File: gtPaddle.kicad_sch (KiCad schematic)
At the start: 57 parts, among them IC1 74157N, Q1 2N3904, Q10 2N3906, Q11 2N3904, Q12 2N3906, Q13 2N3904, Q14 2N3904, Q2 2N3904, Q3 2N3904, Q4 2N3904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

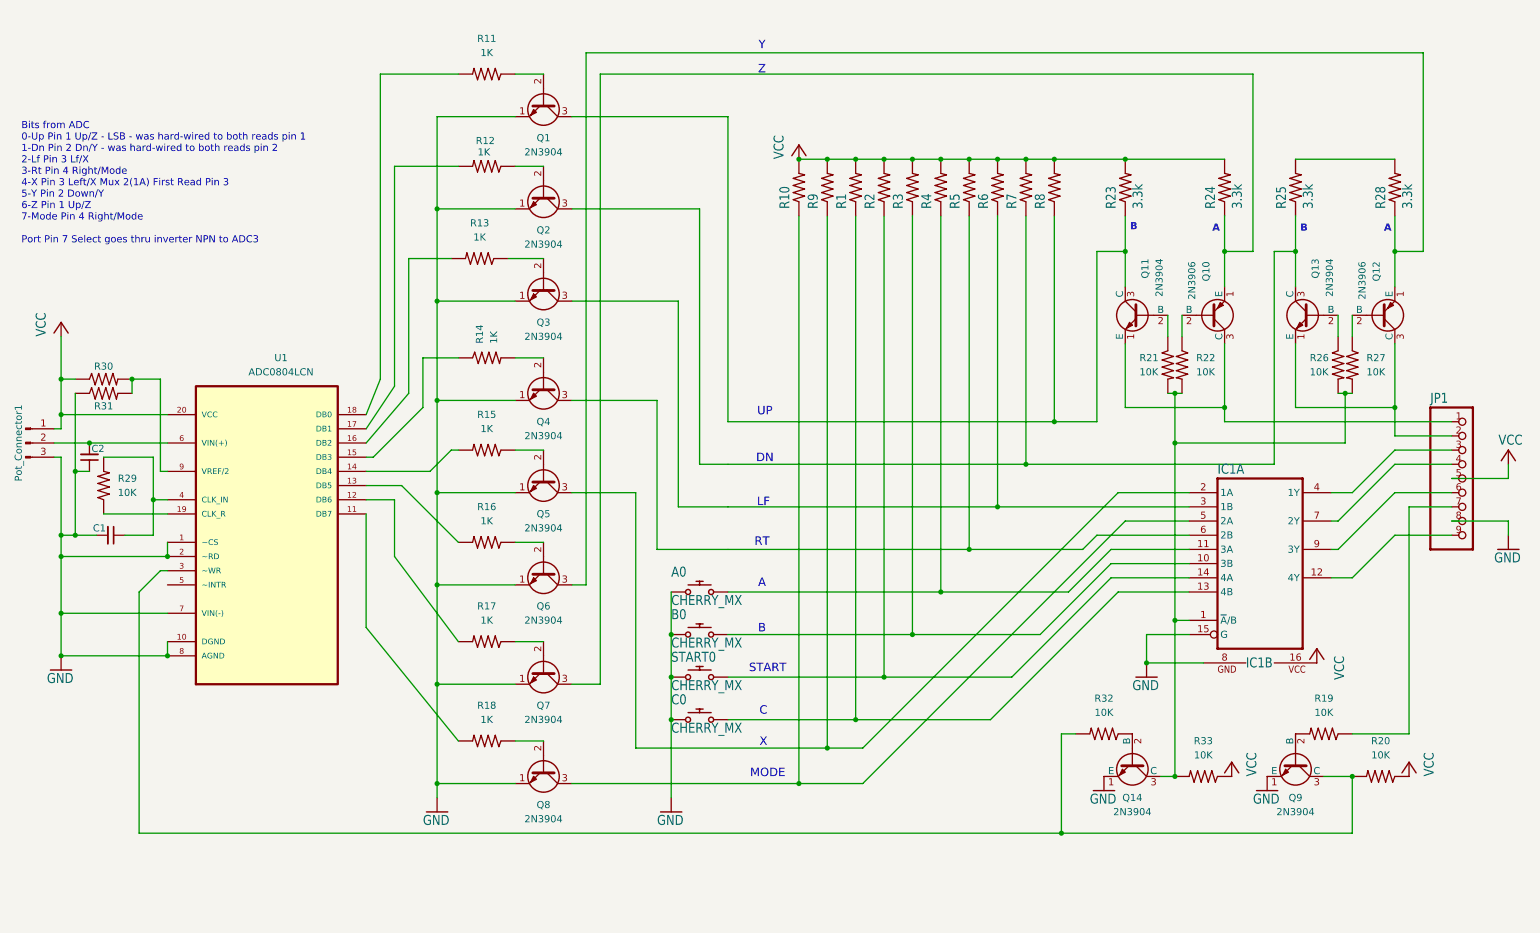
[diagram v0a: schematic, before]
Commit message: much simplified design
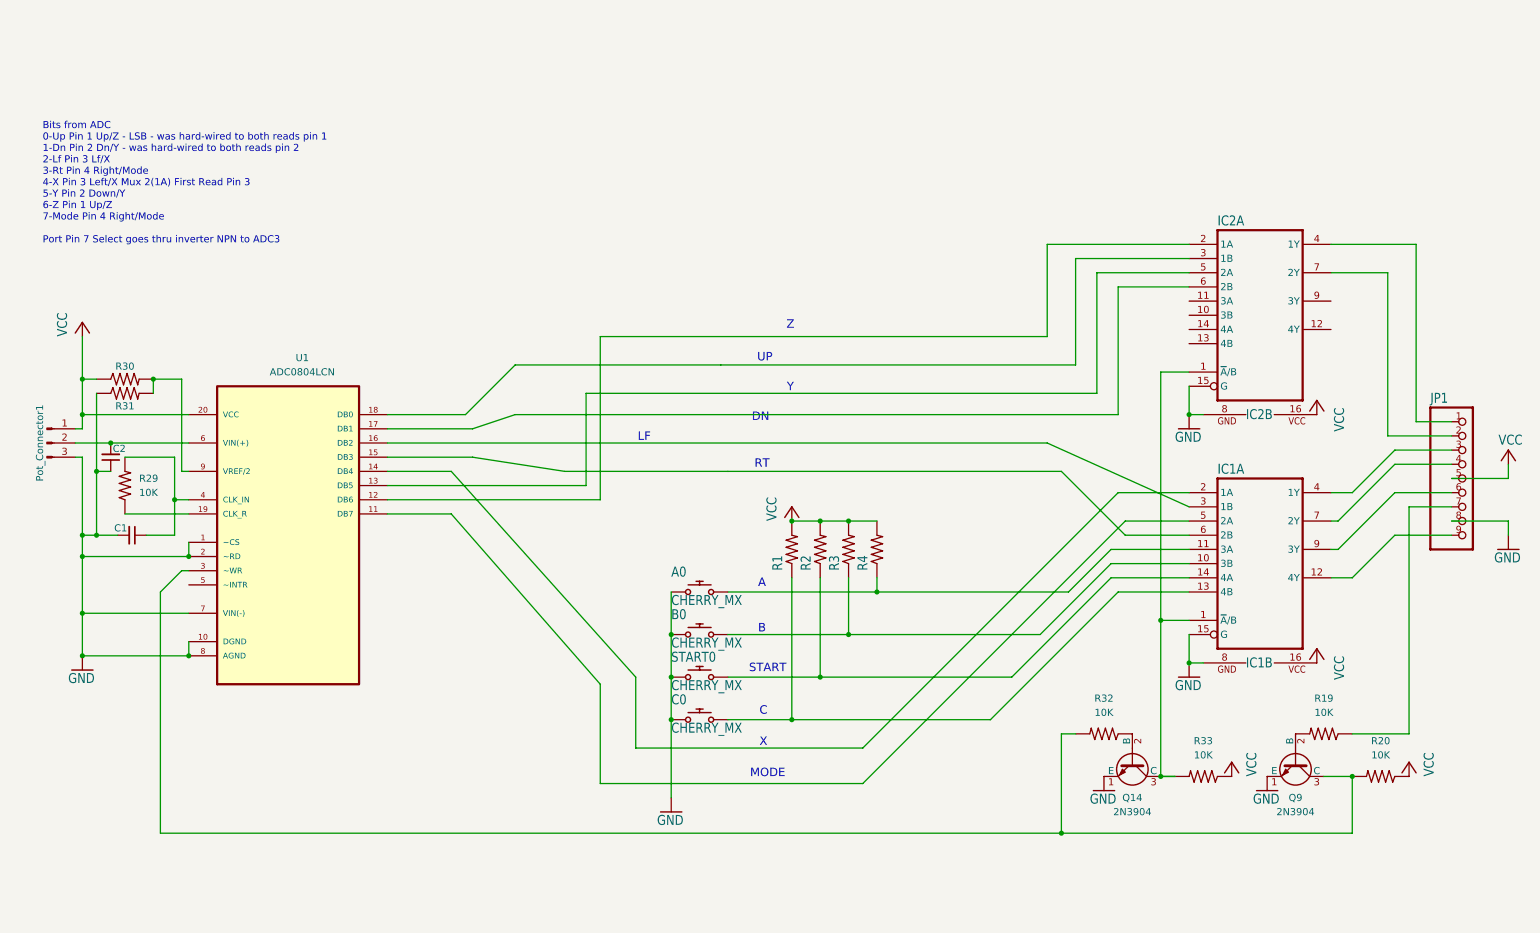
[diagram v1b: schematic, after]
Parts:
- removed Q1, Q11, Q13, Q2, Q3, Q4, Q5, Q6, Q7, Q8: 2N3904, Package_TO_SOT_THT:TO-92_Inline, symbol Transistor_BJT:2N3904
- removed Q10, Q12: 2N3906, Package_TO_SOT_THT:TO-92_Inline, symbol Transistor_BJT:2N3906
- removed R10, R23, R24, R25, R28, R5, R6, R7, R8, R9: 3.3k, gpad1:0207_10, symbol gpad1-eagle-import:R-US_0207/10
- removed R11, R12, R13, R14, R15, R16, R17, R18: 1K, gpad1:0207_10, symbol gpad1-eagle-import:R-US_0207/10
- removed R21, R22, R26, R27: 10K, gpad1:0207_10, symbol gpad1-eagle-import:R-US_0207/10
- added IC2: 74157N, gpad1:DIL16, symbol gpad1-eagle-import:74157N
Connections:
- net GND: now also IC2.15 (G), IC2.8 (GND)
- net VCC: now also IC2.16 (VCC)
- net at IC1.3 (1B): now also U1.16 (DB2)
- net at IC1.1 (~{A}/B), Q14.3 (C), R33.2: now also IC2.1 (~{A}/B)
- net at JP1.1: now also IC2.4 (1Y)
- net at IC1.2 (1A): now also U1.14 (DB4)
- net at U1.13 (DB5): now also IC2.5 (2A)
- net at IC1.5 (2A): now also U1.11 (DB7)
- net at U1.12 (DB6): now also IC2.2 (1A)
- net at U1.17 (DB1): now also IC2.6 (2B)
- net at U1.15 (DB3): now also IC1.6 (2B)
- net at U1.18 (DB0): now also IC2.3 (1B)
- net at JP1.2: now also IC2.7 (2Y)
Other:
- moved on the sheet: C1, C2, Pot_Connector1, R1, R2, R29, R3, R30, R31, R4, U1

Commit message: more simplified
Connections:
- net GND: now also IC2.10 (3B), IC2.11 (3A), IC2.12 (4Y), IC2.13 (4B), IC2.14 (4A), IC2.9 (3Y)
- net at IC1.1 (~{A}/B), IC2.1 (~{A}/B), Q14.3 (C)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: now also IC2.6 (2B), U1.17 (DB1)
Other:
- note added: "Bits from ADC 0-Up Pin 1 Up 1-Dn Pin 2 Dn 2-Lf Pin 3 Lf 3-Rt Pin 4 Right 4-X Pin 3 X Mux 5-Y Pin 2 Y 6-Z Pin 1 Z 7-Mode Pin 4 Mode Port Pin 7 Select goes thru inverter NPN to ADC3 Second inverter as buffer for select just in case"
- note removed: "Bits from ADC 0-Up Pin 1 Up/Z - LSB - was hard-wired to both reads pin 1 1-Dn Pin 2 Dn/Y - was hard-wired to both reads pin 2 2-Lf Pin 3 Lf/X 3-Rt Pin 4 Right/Mode 4-X Pin 3 Left/X Mux 2(1A) First Read Pin 3 5-Y Pin 2 Down/Y 6-Z Pin 1 Up/Z 7-Mode Pin 4 Right/Mode Port Pin 7 Select goes thru inverter NPN to ADC3"
- moved on the sheet: A0, B0, C0, C1, C2, IC1A, IC1B, IC2A, IC2B, JP1, Pot_Connector1, Q14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

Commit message: some wire cleanup
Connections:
- net at IC1.1 (~{A}/B), IC2.1 (~{A}/B), Q14.3 (C)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: no longer IC2.6 (2B), U1.17 (DB1)
- new net: IC2.6 (2B), U1.17 (DB1)
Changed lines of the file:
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@@
 	(text "MODE"
 		(exclude_from_sim no)
-		(at 136.652 88.392 0)
+		(at 135.636 85.344 0)
 		(effects
 			(font
@@
 	(text "RT"
 		(exclude_from_sim no)
-		(at 134.366 78.74 0)
+		(at 134.366 76.962 0)
 		(effects
 			(font
@@
 	(text "X"
 		(exclude_from_sim no)
-		(at 134.62 82.55 0)
+		(at 134.366 80.264 0)
 		(effects
 			(font
@@
 	(text "DN"
 		(exclude_from_sim no)
-		(at 134.112 67.818 0)
+		(at 134.62 64.516 0)
 		(effects
 			(font
@@
 	(text "LF"
 		(exclude_from_sim no)
-		(at 113.284 75.184 0)
+		(at 134.366 72.39 0)
 		(effects
 			(font
@@
 	)
 	(junction
-		(at 205.74 67.31)
-		(diameter 0)
-		(color 0 0 0 0)
-	)
-	(junction
 		(at 187.96 146.05)
 		(diameter 0)
@@
 	)
 	(junction
-		(at 205.74 63.5)
-		(diameter 0)
-		(color 0 0 0 0)
-	)
-	(junction
 		(at 118.11 124.46)
 		(diameter 0)
@@
 	(wire
 		(pts
+			(xy 196.85 64.77) (xy 196.85 57.15)
+		)
+		(stroke
+			(width 0)
+			(type default)
+		)
+	)
+	(wire
+		(pts
 			(xy 39.37 54.61) (xy 58.42 54.61)
 		)
@@
 	(wire
 		(pts
-			(xy 102.87 62.23) (xy 194.31 62.23)
+			(xy 120.65 62.23) (xy 194.31 62.23)
 		)
 		(stroke
@@
 	(wire
 		(pts
-			(xy 205.74 67.31) (xy 205.74 63.5)
+			(xy 190.5 86.36) (xy 194.31 90.17)
 		)
 		(stroke
@@
 	(wire
 		(pts
+			(xy 194.31 85.09) (xy 210.82 85.09)
+		)
+		(stroke
+			(width 0)
+			(type default)
+		)
+	)
+	(wire
+		(pts
 			(xy 240.03 100.33) (xy 247.65 92.71)
 		)
@@
 	(wire
 		(pts
-			(xy 114.3 85.09) (xy 93.98 64.77)
+			(xy 110.49 81.28) (xy 93.98 64.77)
 		)
 		(stroke
@@
 	(wire
 		(pts
+			(xy 196.85 57.15) (xy 205.74 48.26)
+		)
+		(stroke
+			(width 0)
+			(type default)
+		)
+	)
+	(wire
+		(pts
 			(xy 57.15 64.77) (xy 58.42 64.77)
 		)
@@
 	(wire
 		(pts
-			(xy 93.98 72.39) (xy 97.79 72.39)
+			(xy 93.98 72.39) (xy 95.25 72.39)
 		)
 		(stroke
@@
 	(wire
 		(pts
-			(xy 97.79 58.42) (xy 134.62 58.42)
+			(xy 111.76 58.42) (xy 134.62 58.42)
 		)
 		(stroke
@@
 	(wire
 		(pts
-			(xy 205.74 63.5) (xy 205.74 48.26)
-		)
-		(stroke
-			(width 0)
-			(type default)
-		)
-	)
-	(wire
-		(pts
 			(xy 194.31 62.23) (xy 194.31 45.72)
 		)
@@
 	(wire
 		(pts
-			(xy 110.49 78.74) (xy 93.98 62.23)
+			(xy 113.03 77.47) (xy 96.52 62.23)
 		)
 		(stroke
@@
 	(wire
 		(pts
-			(xy 97.79 58.42) (xy 93.98 54.61)
-		)
-		(stroke
-			(width 0)
-			(type default)
-		)
-	)
-	(wire
-		(pts
-			(xy 110.49 78.74) (xy 175.26 78.74)
+			(xy 111.76 58.42) (xy 107.95 54.61)
+		)
+		(stroke
+			(width 0)
+			(type default)
+		)
+	)
+	(wire
+		(pts
+			(xy 113.03 77.47) (xy 167.64 77.47)
 		)
 		(stroke
@@
 	(wire
 		(pts
-			(xy 205.74 67.31) (xy 205.74 107.95)
-		)
-		(stroke
-			(width 0.1524)
-			(type solid)
-		)
-	)
-	(wire
-		(pts
 			(xy 190.5 43.18) (xy 210.82 43.18)
 		)
@@
 	(wire
 		(pts
-			(xy 205.74 63.5) (xy 205.74 67.31)
+			(xy 205.74 63.5) (xy 205.74 107.95)
 		)
 		(stroke
@@
 	(wire
 		(pts
+			(xy 101.6 57.15) (xy 93.98 57.15)
+		)
+		(stroke
+			(width 0)
+			(type default)
+		)
+	)
+	(wire
+		(pts
+			(xy 194.31 85.09) (xy 190.5 81.28)
+		)
+		(stroke
+			(width 0)
+			(type default)
+		)
+	)
+	(wire
+		(pts
 			(xy 210.82 115.57) (xy 213.36 115.57)
 		)
@@
 	(wire
 		(pts
-			(xy 175.26 78.74) (xy 186.69 92.71)
+			(xy 167.64 77.47) (xy 179.07 92.71)
 		)
 		(stroke
@@
 	(wire
 		(pts
-			(xy 97.79 72.39) (xy 115.57 90.17)
+			(xy 95.25 72.39) (xy 113.03 86.36)
 		)
 		(stroke
@@
 	(wire
 		(pts
-			(xy 93.98 67.31) (xy 97.79 67.31)
+			(xy 93.98 67.31) (xy 115.57 67.31)
 		)
 		(stroke
@@
 	(wire
 		(pts
-			(xy 104.14 67.31) (xy 205.74 67.31)
+			(xy 110.49 64.77) (xy 196.85 64.77)
 		)
 		(stroke
@@
 	(wire
 		(pts
-			(xy 114.3 85.09) (xy 210.82 85.09)
+			(xy 110.49 81.28) (xy 190.5 81.28)
 		)
 		(stroke
@@
 	(wire
 		(pts
+			(xy 107.95 54.61) (xy 93.98 54.61)
+		)
+		(stroke
+			(width 0)
+			(type default)
+		)
+	)
+	(wire
+		(pts
 			(xy 234.95 135.89) (xy 240.03 135.89)
 		)
@@
 	(wire
 		(pts
-			(xy 104.14 67.31) (xy 93.98 57.15)
+			(xy 203.2 87.63) (xy 189.23 73.66)
+		)
+		(stroke
+			(width 0.1524)
+			(type solid)
+		)
+	)
+	(wire
+		(pts
+			(xy 110.49 64.77) (xy 101.6 57.15)
 		)
 		(stroke
@@
 	(wire
 		(pts
-			(xy 110.49 76.2) (xy 93.98 59.69)
-		)
-		(stroke
-			(width 0.1524)
-			(type solid)
-		)
-	)
-	(wire
-		(pts
-			(xy 200.66 90.17) (xy 210.82 90.17)
+			(xy 97.79 59.69) (xy 93.98 59.69)
+		)
+		(stroke
+			(width 0.1524)
+			(type solid)
+		)
+	)
+	(wire
+		(pts
+			(xy 114.3 73.66) (xy 97.79 59.69)
 		)
 		(stroke
@@
 	(wire
 		(pts
-			(xy 186.69 92.71) (xy 210.82 92.71)
-		)
-		(stroke
-			(width 0.1524)
-			(type solid)
-		)
-	)
-	(wire
-		(pts
-			(xy 115.57 90.17) (xy 200.66 90.17)
+			(xy 179.07 92.71) (xy 210.82 92.71)
+		)
+		(stroke
+			(width 0.1524)
+			(type solid)
+		)
+	)
+	(wire
+		(pts
+			(xy 113.03 86.36) (xy 190.5 86.36)
 		)
 		(stroke
@@
 	(wire
 		(pts
-			(xy 210.82 87.63) (xy 185.42 76.2)
-		)
-		(stroke
-			(width 0.1524)
-			(type solid)
-		)
-	)
-	(wire
-		(pts
 			(xy 144.78 106.68) (xy 144.78 124.46)
 		)
@@
 	(wire
 		(pts
-			(xy 97.79 67.31) (xy 102.87 62.23)
+			(xy 115.57 67.31) (xy 120.65 62.23)
 		)
 		(stroke
@@
 	(wire
 		(pts
-			(xy 110.49 76.2) (xy 185.42 76.2)
+			(xy 114.3 73.66) (xy 189.23 73.66)
 		)
 		(stroke
@@
 	(wire
 		(pts
+			(xy 203.2 87.63) (xy 210.82 87.63)
+		)
+		(stroke
+			(width 0.1524)
+			(type solid)
+		)
+	)
+	(wire
+		(pts
 			(xy 257.81 82.55) (xy 267.97 82.55)
 		)
@@
 	(wire
 		(pts
+			(xy 194.31 90.17) (xy 210.82 90.17)
+		)
+		(stroke
+			(width 0.1524)
+			(type solid)
+		)
+	)
+	(wire
+		(pts
 			(xy 44.45 59.69) (xy 58.42 59.69)
 		)
@@
 		)
 	)
+	(wire
+		(pts
+			(xy 96.52 62.23) (xy 93.98 62.23)
+		)
+		(stroke
+			(width 0.1524)
+			(type solid)
+		)
+	)

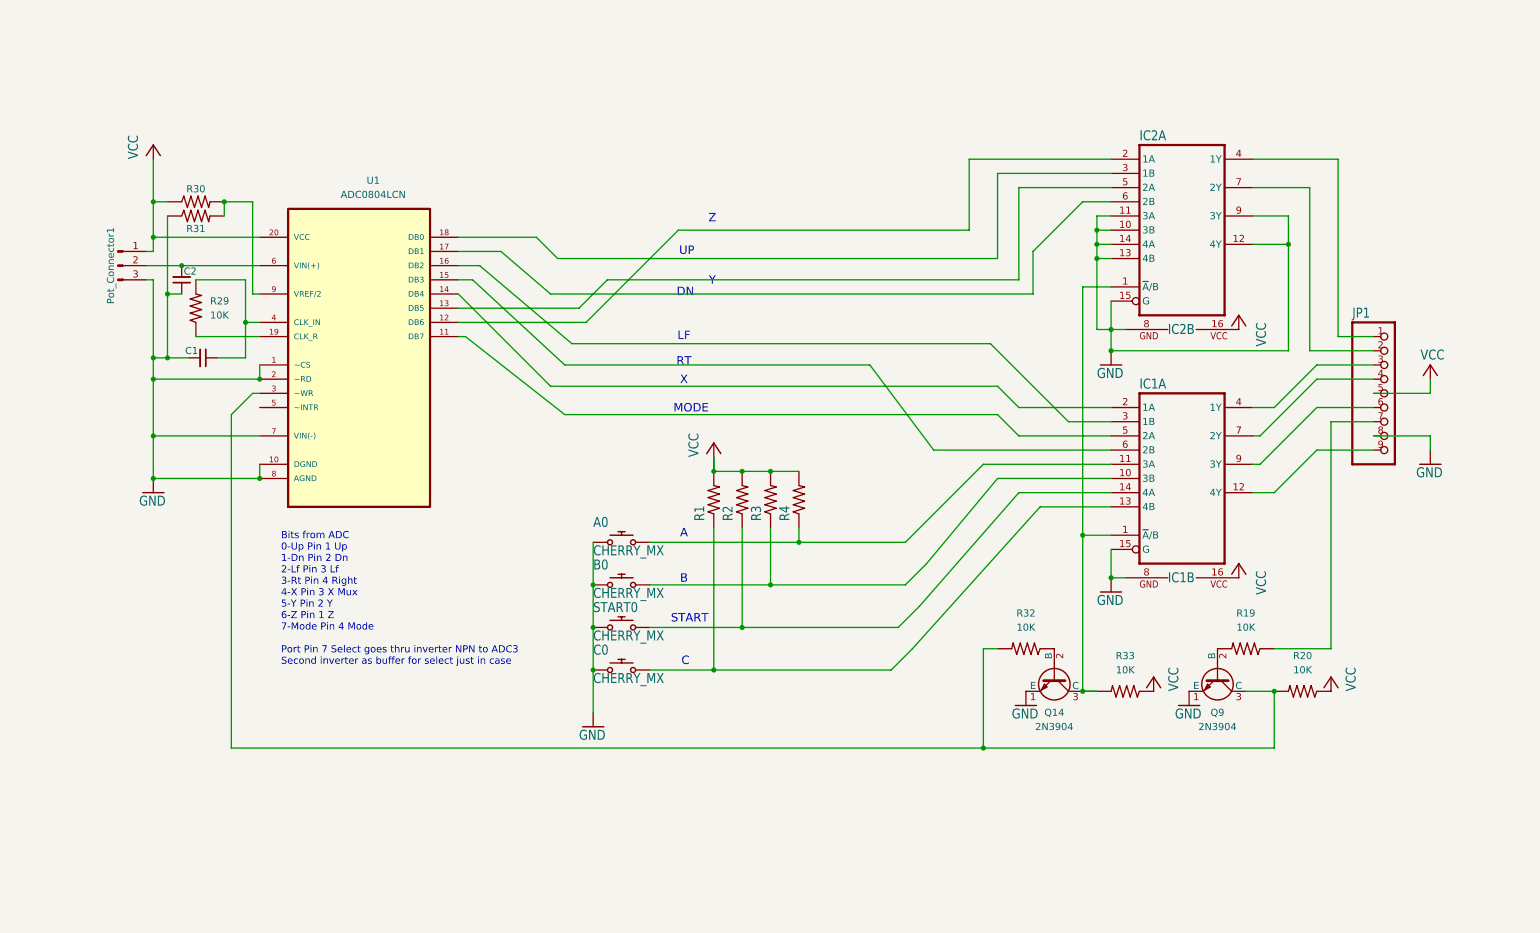
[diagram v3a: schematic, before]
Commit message: remove second inverter from select
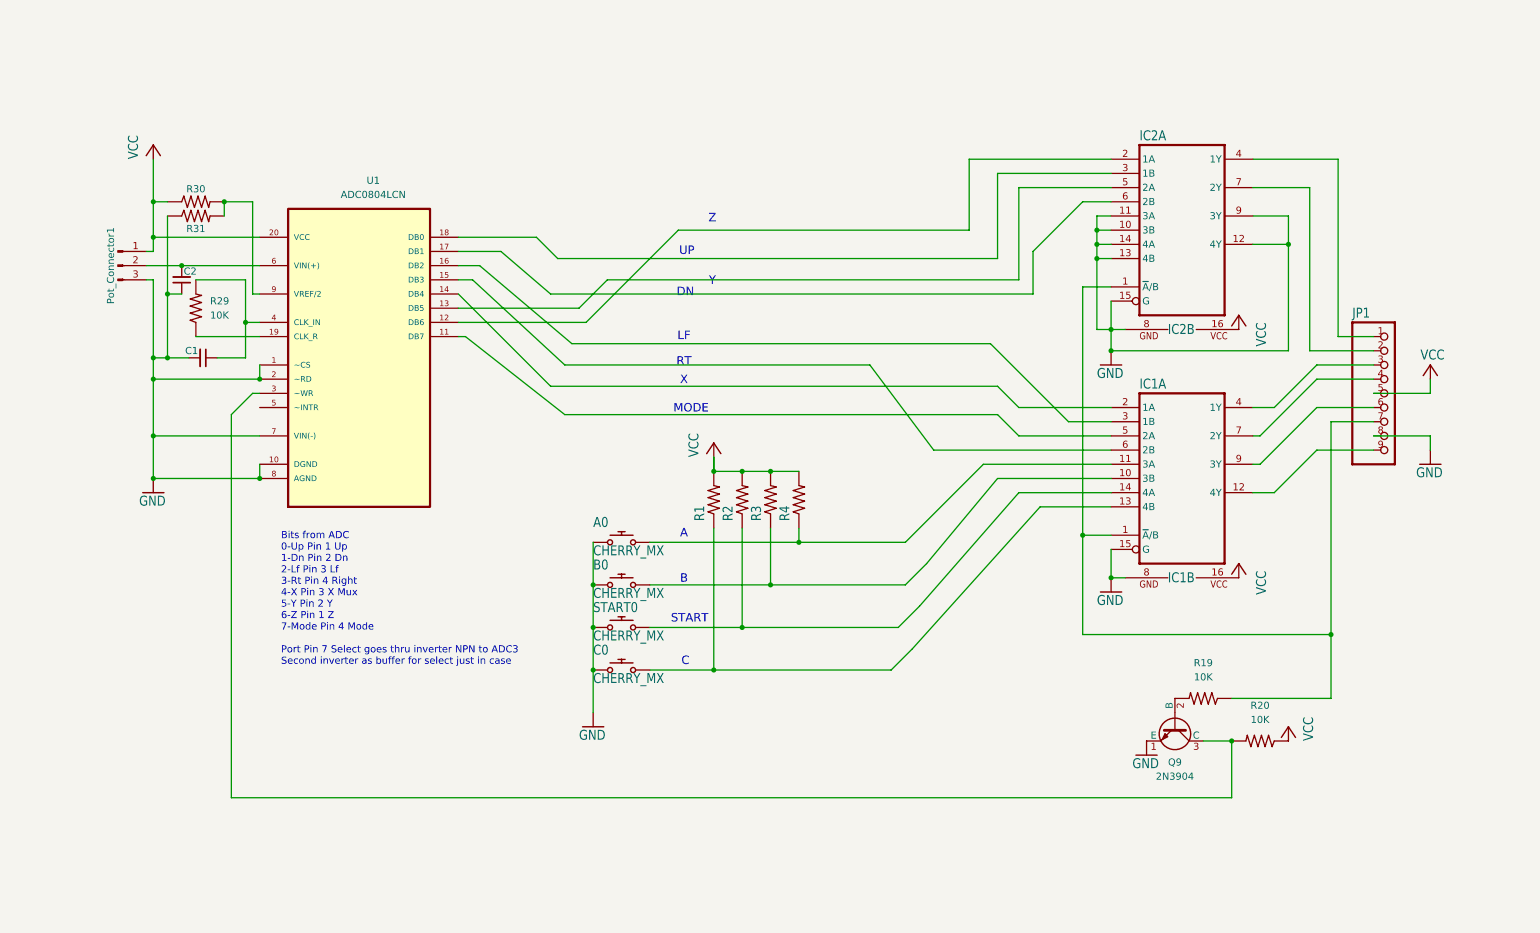
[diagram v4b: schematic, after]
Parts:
- removed Q14: 2N3904, Package_TO_SOT_THT:TO-92_Inline, symbol Transistor_BJT:2N3904
- removed R32, R33: 10K, gpad1:0207_10, symbol gpad1-eagle-import:R-US_0207/10
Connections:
- net at IC1.1 (~{A}/B), IC2.1 (~{A}/B): now also JP1.7, R19.1
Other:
- moved on the sheet: Q9, R19, R20
